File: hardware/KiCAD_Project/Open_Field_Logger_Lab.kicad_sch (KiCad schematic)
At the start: 61 parts, among them J1 1-0001899, J10 1-0001899, J11 1-0001899, J12 1-0001899, J13 1-0001899, J14 1-0001899, J2 1-0001894, J3 1-0001894, J4 AUX Input, J5 NP_Conn_01x03, J6 NP_Conn_01x06, J7 NP_Conn_01x04, J8 1-0000127, J9 Conn_01x01, Q1 1-0000163, Q2 1-0000163, Q3 1-0000163, SW1 1-0000681, U1 1-0001893, U2 1-0001890, U3 1-0001892, U4 1-0001891, Y1 1-0001901

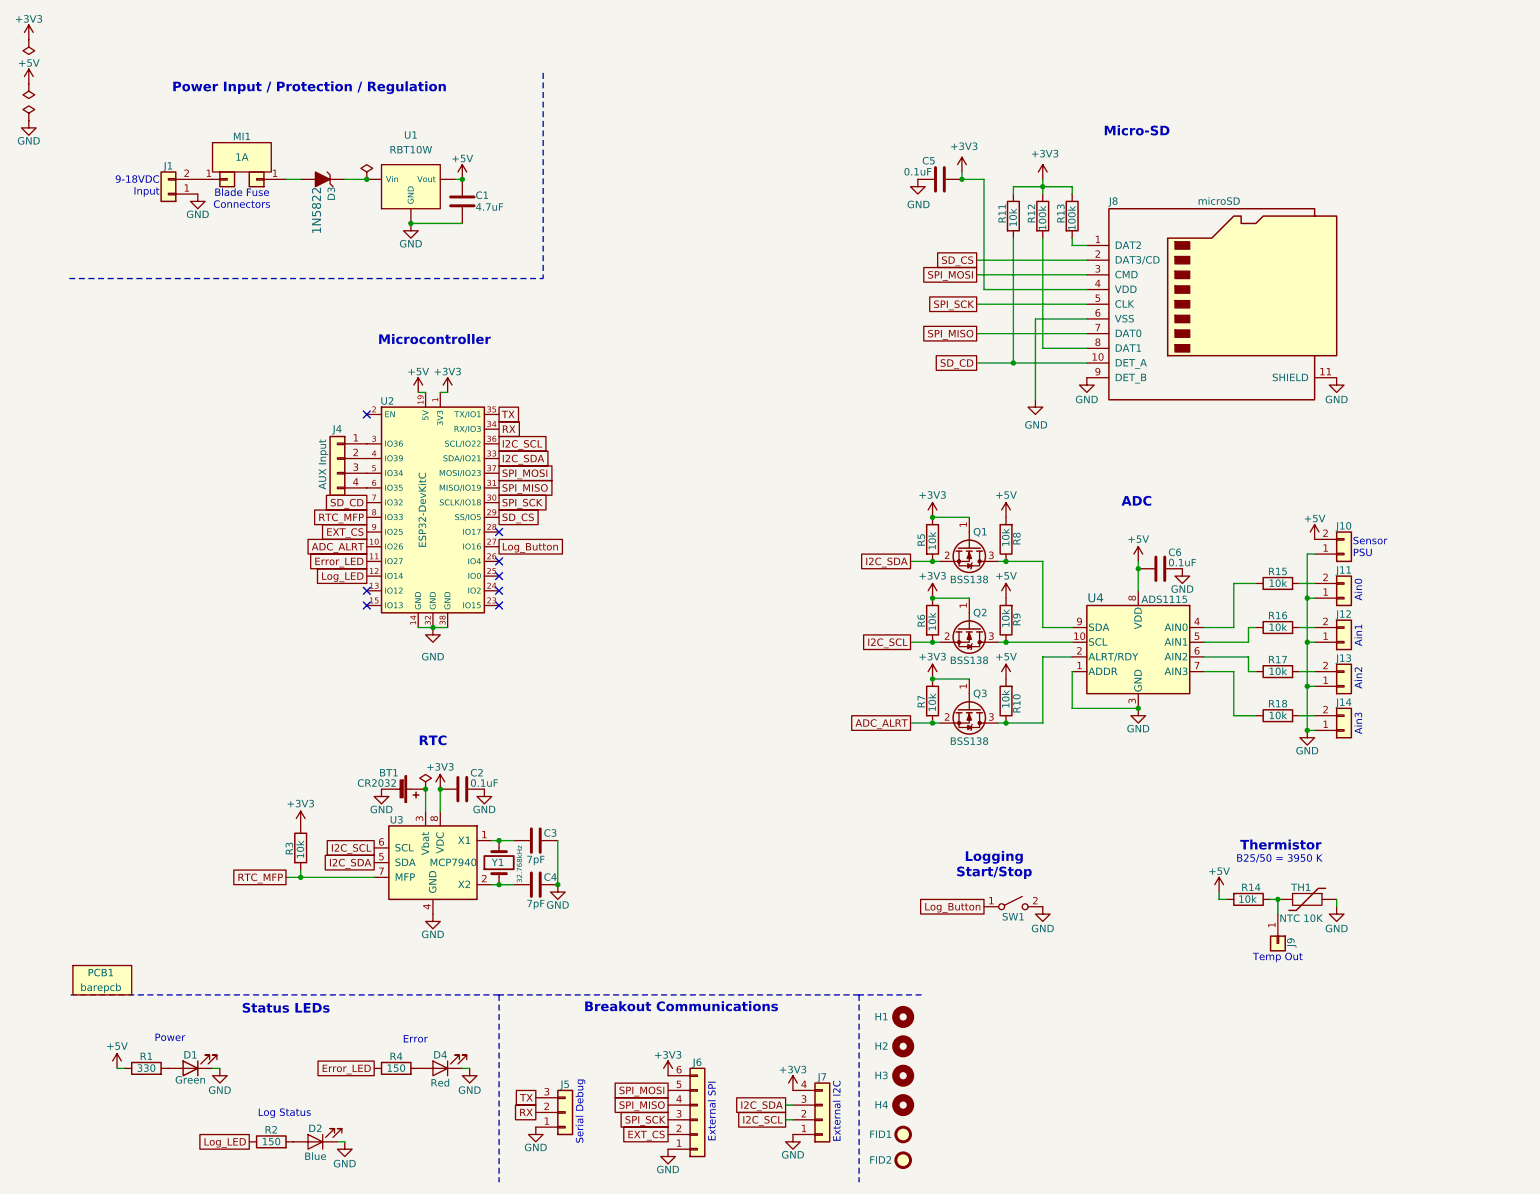
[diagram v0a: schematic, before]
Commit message: Rev 1.2 Redesign: Major Changes: - Switch to SMD ESP32-S3 with updated GPIO mapping - Added 3.3V regulation and USB-C Powering - Added dual-source power support - Replaced RTC battery with 1F supercap - Replaced microSD with SPI Flash - Updated supporting circuitry
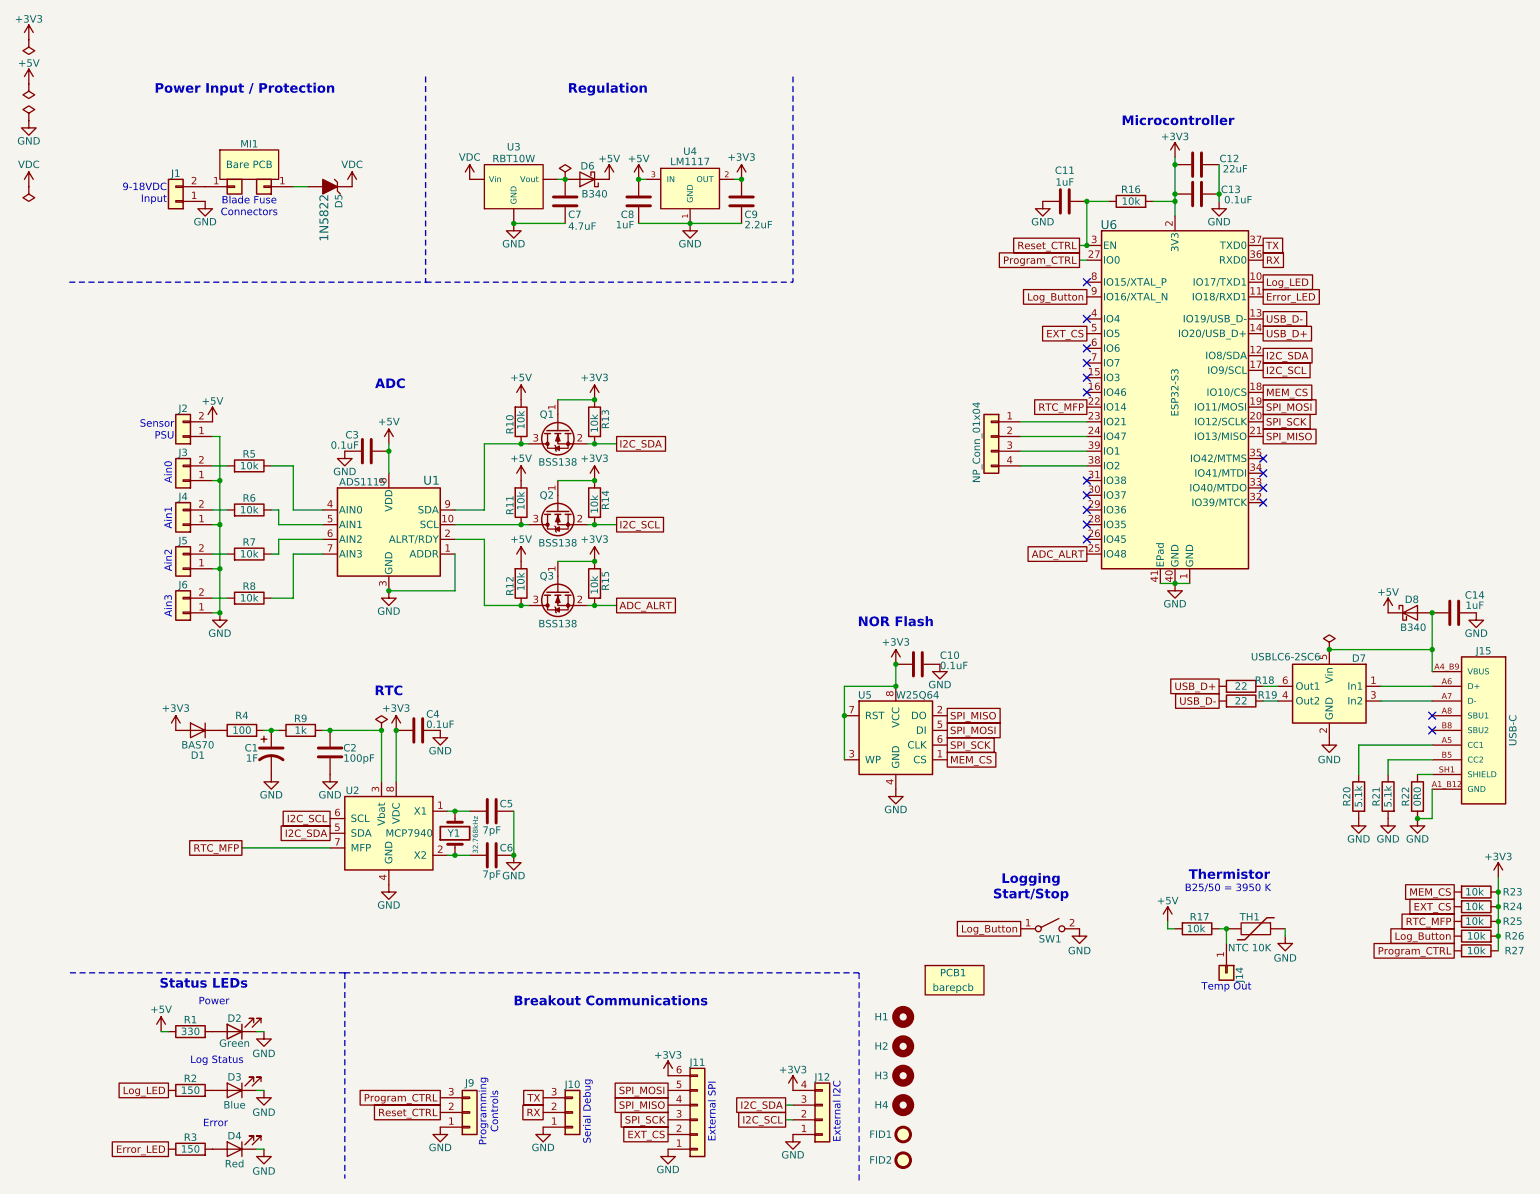
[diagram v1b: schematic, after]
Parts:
- removed BT1: 1-0000863, batteries:1-0000863, symbol batteries:1-0000863
- removed C5: 1-0000007, capacitors_0603:1-0000007, symbol capacitors_0603:1-0000007
- removed J8: 1-0000127, connectors:1-0000127, symbol connectors:1-0000127
- removed R11: 1-0000010, resistors_0603:1-0000010, symbol resistors_0603:1-0000010
- removed R12, R13: 1-0000174, resistors_0603:1-0000174, symbol resistors_0603:1-0000174
- removed U2: 1-0001890, microcontrollers:1-0001890, symbol microcontrollers:1-0001890
- added C1: 1-0001956, capacitors_th:1-0001956, symbol capacitors_th:1-0001956
- added C10, C13: 1-0000007, capacitors_0603:1-0000007, symbol capacitors_0603:1-0000007
- added C11, C14, C8: 1-0000018, capacitors_0603:1-0000018, symbol capacitors_0603:1-0000018
- added C12: 1-0000015, capacitors_0603:1-0000015, symbol capacitors_0603:1-0000015
- added C2: 1-0000904, capacitors_0603:1-0000904, symbol capacitors_0603:1-0000904
- added C9: 1-0000324, capacitors_0603:1-0000324, symbol capacitors_0603:1-0000324
- added D1: 1-0001955, diodes:1-0001955, symbol diodes:1-0001955
- added D6, D8: 1-0001977, diodes:1-0001977, symbol diodes:1-0001977
- added D7: 1-0001931, diodes:1-0001931, symbol diodes:1-0001931
- added J15: 1-0001974, connectors:1-0001974, symbol connectors:1-0001974
- added J9: NP_Conn_01x03, np_connectors:PinHeader_1x03_P2.54mm_Vertical, symbol np_connectors:NP_Conn_01x03
- added R16, R23, R24, R26, R27: 1-0000010, resistors_0603:1-0000010, symbol resistors_0603:1-0000010
- added R18, R19: 1-0001933, resistors_0603:1-0001933, symbol resistors_0603:1-0001933
- added R20, R21: 1-0001859, resistors_0603:1-0001859, symbol resistors_0603:1-0001859
- added R22: 1-0000006, resistors_0603:1-0000006, symbol resistors_0603:1-0000006
- added R4: 1-0000112, resistors_0603:1-0000112, symbol resistors_0603:1-0000112
- added R9: 1-0000013, resistors_0603:1-0000013, symbol resistors_0603:1-0000013
- added U4: 1-0001973, regulators:1-0001973, symbol regulators:1-0001973
- added U5: 1-0001976, eeproms:1-0001976, symbol eeproms:1-0001976
- added U6: 1-0001927, microcontrollers:1-0001927, symbol microcontrollers:1-0001927
- D2: renamed from D1; Populated 0 -> 1
- D5: renamed from D3; Populated 0 -> 1
- J1: Populated 0 -> 1
- J13: renamed from J4; PValue AUX Input -> NP_Conn_01x04
- J2: renamed from J10; Populated 0 -> 1
- J3: renamed from J11; Populated 0 -> 1
- J4: renamed from J12; Populated 0 -> 1
- J5: renamed from J13; Populated 0 -> 1
- J6: renamed from J14; Populated 0 -> 1
- MI1: Internal Part Number 1-0001895 -> 0-0000000; PValue 1A -> Bare PCB
- PCB1: Internal Part Number 3-0000307 -> 3-0000321
- TH1: PValue NTC 10K -> NTC 10K; Populated 0 -> 1
- U2: renamed from U3; Populated 0 -> 1
- U3: renamed from U1; Populated 0 -> 1
- renumbered C6 to C3, C2 to C4, C3 to C5, C4 to C6, C1 to C7, D2 to D3, J5 to J10, J6 to J11, J7 to J12, J9 to J14, J2 to J7, J3 to J8, R8 to R10, R9 to R11, R10 to R12, R5 to R13, R6 to R14, R7 to R15, R14 to R17, R3 to R25, R4 to R3, R15 to R5, R16 to R6, R17 to R7, R18 to R8, U4 to U1
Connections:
- net +3V3: now also C10.1, C12.1, C13.1, C9.1, D1.1 (A), R16.2, R23.1, R24.1, R26.2, R27.1, U4.2 (OUT), U4.4, U5.3 (WP), U5.7 (RST), U5.8 (VCC), U6.2 (3V3)
- net +5V: now also C8.1, D6.1 (K), D8.1 (K), U4.3 (IN); no longer C7.1, U3.3 (Vout)
- net ADC_ALRT: now also U6.25 (IO48)
- net EXT_CS: now also R24.2, U6.5 (IO5)
- net Error_LED: now also U6.11 (IO18/RXD1)
- net GND: now also C1.2, C10.2, C11.1, C12.2, C13.2, C14.2, C2.2, C8.2, C9.2, D7.2 (GND), J15.A1_B12 (GND), J15.B1_A12 (GND), J9.1 (Pin_1), R20.2, R21.2, R22.2, U4.1 (GND), U5.4 (GND), U6.1 (GND), U6.40 (GND), U6.41 (EPad), U6.42 (GND), U6.43 (GND), U6.44 (GND), U6.45 (GND), U6.46 (GND), U6.47 (GND), U6.48 (GND), U6.49 (GND)
- net I2C_SCL: now also U6.17 (IO9/SCL)
- net I2C_SDA: now also U6.12 (IO8/SDA)
- net Log_Button: now also R26.1, U6.9 (IO16/XTAL_N)
- net Log_LED: now also U6.10 (IO17/TXD1)
- net RTC_MFP: now also U6.22 (IO14)
- net RX: now also U6.36 (RXD0)
- net SPI_MISO: now also U5.2 (DO), U6.21 (IO13/MISO)
- net SPI_MOSI: now also U5.5 (DI), U6.19 (IO11/MOSI)
- net SPI_SCK: now also U5.6 (CLK), U6.20 (IO12/SCLK)
- net TX: now also U6.37 (TXD0)
- net VDC: now reaches D5.1, U3.1 (Vin)
- net at U2.3 (Vbat): now also C2.1, R9.2
- net at J13.1 (Pin_1): now also U6.23 (IO21)
- net at J13.2 (Pin_2): now also U6.24 (IO47)
- net at J13.3 (Pin_3): now also U6.39 (IO1)
- net at J13.4 (Pin_4): now also U6.38 (IO2)
- new net: D1.3 (K), R4.1
- new net: C1.1, R4.2, R9.1
- new net: J15.SH1 (SHIELD), J15.SH2 (SHIELD), J15.SH3 (SHIELD), J15.SH4 (SHIELD), R22.1
- new net: C7.1, D6.2 (A), U3.3 (Vout)
- new net: D7.6 (Out1), R18.1
- new net: D7.4 (Out2), R19.1
- new net: D7.1 (In1), J15.A6 (D+), J15.B6 (D+)
- new net: D7.3 (In2), J15.A7 (D-), J15.B7 (D-)
- new net: J15.A5 (CC1), R20.1
- new net: J15.B5 (CC2), R21.1
- new net MEM_CS: R23.2, U5.1 (CS), U6.18 (IO10/CS)
- new net Program_CTRL: J9.3 (Pin_3), R27.2, U6.27 (IO0)
- new net Reset_CTRL: C11.2, J9.2 (Pin_2), R16.1, U6.3 (EN)
- new net USB_D+: R18.2, U6.14 (IO20/USB_D+)
- new net USB_D-: R19.2, U6.13 (IO19/USB_D-)
- new net VBUS: C14.1, D7.5 (Vin), D8.2 (A), J15.A4_B9 (VBUS), J15.B4_A9 (VBUS)
- no-connect marks 8 -> 17
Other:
- note added: "NOR Flash"
- note added: "Power Input / Protection"
- note added: "Programming Controls"
- note added: "Regulation"
- note removed: "Micro-SD"
- note removed: "Power Input / Protection / Regulation"
- moved on the sheet: C3, C4, C5, C6, C7, D2, D3, D4, D5, J1, J10, J14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
